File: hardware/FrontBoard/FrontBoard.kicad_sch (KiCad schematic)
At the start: 0 parts

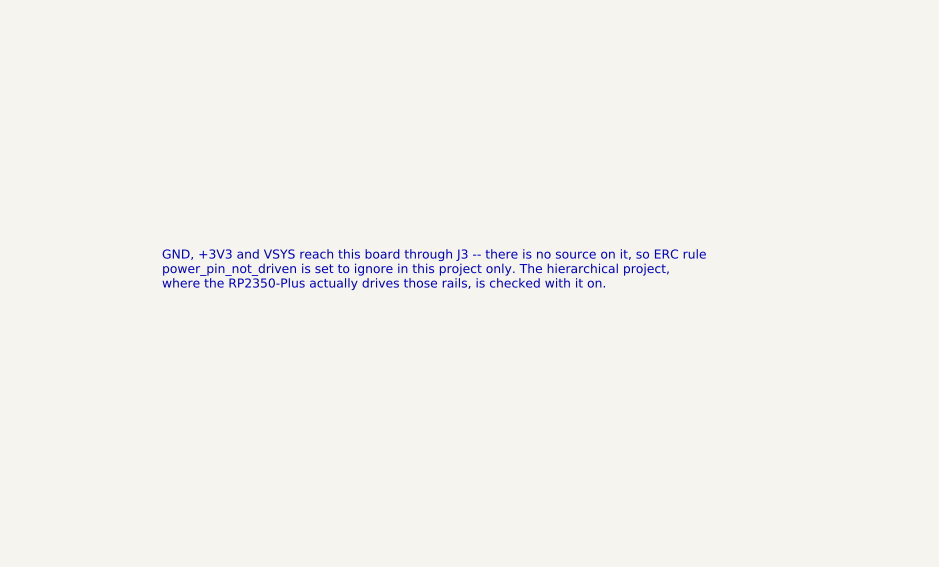
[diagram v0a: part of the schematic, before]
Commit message: The boards are drawn for a Pico 2, not for what I had written
Michael's correction: the target is a plain Raspberry Pi Pico 2, the
module most of the instruments here run on, and the Waveshare RP2350-Plus
is what goes in when 16 MB of flash is wanted. "WeAct" was my own
invention -- the top-level README has said Waveshare all along.

That flips the standing caveat on the spring pin. TP2's position comes
from the Pico 2 datasheet, so it is the drawn-for part's own document
rather than a number borrowed from a different board. Only the side of the
centreline was ever unsettled, because a drawing does not say which face
it is viewed from, and that is now checked on the part: nearer the GP0
row, which is the 26.51 already there.

What moves to the Waveshare board instead is the whole caveat: different
PCB, its BOOT pad is elsewhere, and that build uses TP1 and a wire. Which
is what TP1 is for. No board change to switch -- you fit either the pin or
the wire.

Also dropped a resistor designator that came from the wrong schematic, and
the note in the schematic now names TP6, TP2 and TP1 and says which build
takes which.

Co-Authored-By: Claude Opus 5 <noreply@anthropic.com>
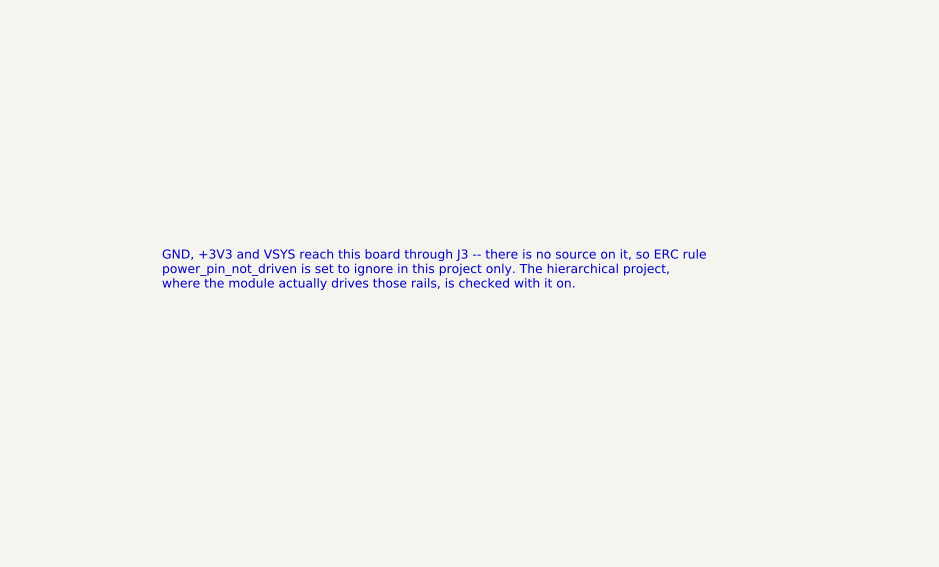
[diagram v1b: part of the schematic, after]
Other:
- note added: "GND, +3V3 and VSYS reach this board through J3 -- there is no source on it, so ERC rule power_pin_not_driven is set to ignore in this project only. The hierarchical project, where the module actually drives those rails, is checked with it on."
- note removed: "GND, +3V3 and VSYS reach this board through J3 -- there is no source on it, so ERC rule power_pin_not_driven is set to ignore in this project only. The hierarchical project, where the RP2350-Plus actually drives those rails, is checked with it on."
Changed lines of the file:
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@@
 	)
 	(embedded_fonts no)
-	(text "GND, +3V3 and VSYS reach this board through J3 -- there is no source on it, so ERC rule\npower_pin_not_driven is set to ignore in this project only. The hierarchical project,\nwhere the RP2350-Plus actually drives those rails, is checked with it on."
+	(text "GND, +3V3 and VSYS reach this board through J3 -- there is no source on it, so ERC rule\npower_pin_not_driven is set to ignore in this project only. The hierarchical project,\nwhere the module actually drives those rails, is checked with it on."
 		(exclude_from_sim no)
 		(at 168.0 92.0 0)
